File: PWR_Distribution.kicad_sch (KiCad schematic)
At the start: 33 parts, among them IC4 AP64501QSP-13, IC8 LM76202QPWPRQ1, J1 CarPowerConnector

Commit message: fixed erc and removed old schematics
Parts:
- IC8: Arrow Part Number (none) -> LM76202QPWPRQ1; Arrow Price/Stock (none) -> https://www.arrow.com/en/products/lm76202qpwprq1/texas-inst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; Height (none) -> 1.2; Manufacturer_Name (none) -> Texas Instruments; Manufacturer_Part_Number (none) -> LM76202QPWPRQ1; Mouser Part Number (none) -> 595-LM76202QPWPRQ1; Mouser Price/Stock (none) -> https://www.mouser.co.uk/ProductDetail/Texas-Instruments/LM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

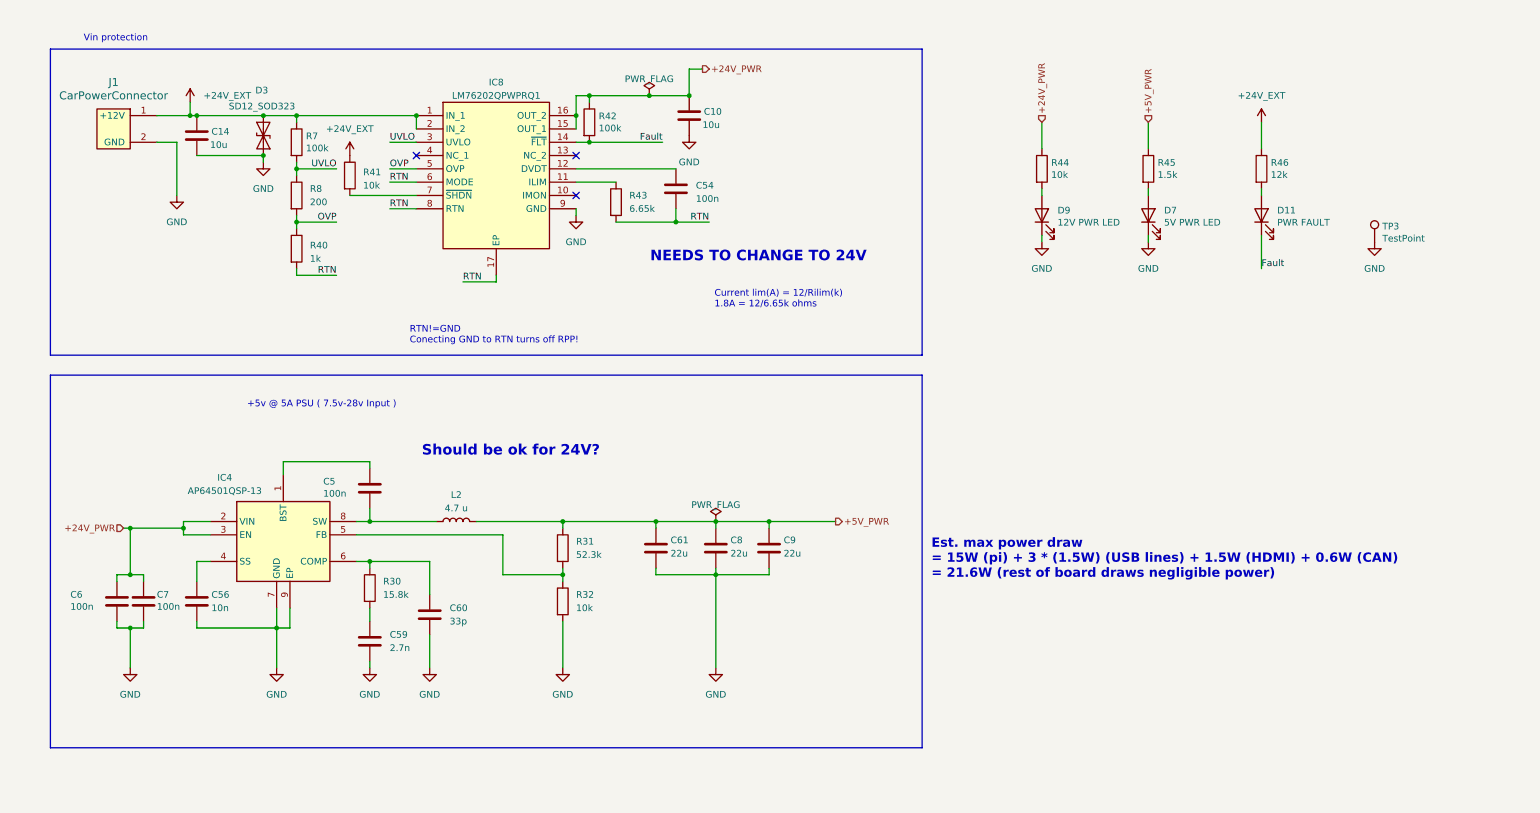
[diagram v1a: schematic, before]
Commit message: updated power to 24V i think
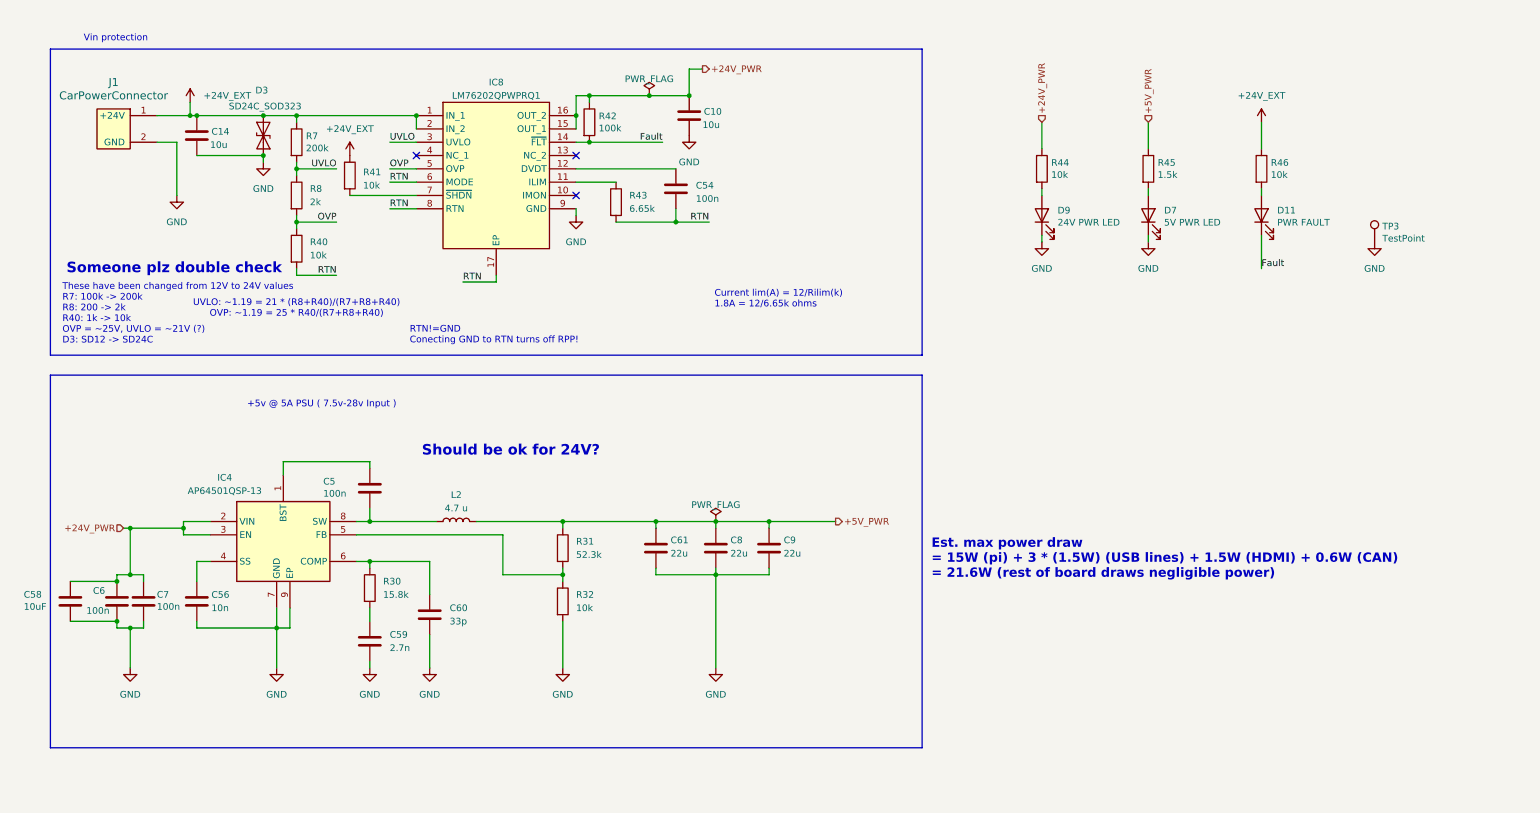
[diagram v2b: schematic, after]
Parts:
- added C58: 10uF, Capacitor_SMD:C_0805_2012Metric, symbol Device:C
- D3: value SD12_SOD323 -> SD24C_SOD323; P/N PESD15VL1BA,115 -> SD24C-01FTG
- D9: value 12V PWR LED -> 24V PWR LED
- R40: value 1k -> 10k
- R46: value 12k -> 10k
- R7: value 100k -> 200k
- R8: value 200 -> 2k
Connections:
- net +24V_PWR: now also C58.1
- net GND: now also C58.2
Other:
- note added: "Someone plz double check"
- note added: "These have been changed from 12V to 24V values R7: 100k -> 200k R8: 200 -> 2k R40: 1k -> 10k OVP = ~25V, UVLO = ~21V (?) D3: SD12 -> SD24C"
- note added: "UVLO: ~1.19 = 21 * (R8+R40)/(R7+R8+R40) OVP: ~1.19 = 25 * R40/(R7+R8+R40)"
- note removed: "NEEDS TO CHANGE TO 24V"
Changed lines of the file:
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@@
 		)
 	)
+	(text "UVLO: ~1.19 = 21 * (R8+R40)/(R7+R8+R40)\nOVP: ~1.19 = 25 * R40/(R7+R8+R40)"
+		(exclude_from_sim no)
+		(at 67.31 74.93 0)
+		(effects
+			(font
+				(size 1.27 1.27)
+			)
+		)
+	)
+	(text "These have been changed from 12V to 24V values\nR7: 100k -> 200k\nR8: 200 -> 2k\nR40: 1k -> 10k\nOVP = ~25V, UVLO = ~21V (?)\nD3: SD12 -> SD24C"
+		(exclude_from_sim no)
+		(at 22.606 75.946 0)
+		(effects
+			(font
+				(size 1.27 1.27)
+			)
+			(justify left)
+		)
+	)
 	(text "Est. max power draw \n= 15W (pi) + 3 * (1.5W) (USB lines) + 1.5W (HDMI) + 0.6W (CAN) \n= 21.6W (rest of board draws negligible power)\n"
 		(exclude_from_sim no)
@@
 		)
 	)
-	(text "NEEDS TO CHANGE TO 24V"
+	(text "Someone plz double check\n"
 		(exclude_from_sim no)
-		(at 155.448 65.024 0)
+		(at 43.942 67.31 0)
 		(effects
 			(font
@@
 	)
 	(junction
+		(at 33.02 134.62)
+		(diameter 0)
+		(color 0 0 0 0)
+	)
+	(junction
 		(at 45.72 116.84)
 		(diameter 0)
@@
 	)
 	(junction
+		(at 33.02 127)
+		(diameter 0)
+		(color 0 0 0 0)
+	)
+	(junction
 		(at 134.62 34.29)
 		(diameter 0)
@@
 	(wire
 		(pts
+			(xy 24.13 127) (xy 33.02 127)
+		)
+		(stroke
+			(width 0)
+			(type default)
+		)
+	)
+	(wire
+		(pts
 			(xy 134.62 34.29) (xy 142.24 34.29)
 		)
@@
 	(wire
 		(pts
+			(xy 24.13 134.62) (xy 33.02 134.62)
+		)
+		(stroke
+			(width 0)
+			(type default)
+		)
+	)
+	(wire
+		(pts
 			(xy 67.31 67.31) (xy 67.31 68.58)
 		)
@@
 			)
 		)
-		(property "Value" "100k"
+		(property "Value" "200k"
 			(at 69.088 44.323 0)
 			(effects
@@
 			)
 		)
-		(property "Value" "12V PWR LED"
+		(property "Value" "24V PWR LED"
 			(at 212.5472 58.4962 90)
 			(effects
@@
 			)
 		)
-		(property "Value" "200"
+		(property "Value" "2k"
 			(at 69.85 54.6099 0)
 			(effects
@@
 			)
 		)
-		(property "Value" "SD12_SOD323"
+		(property "Value" "SD24C_SOD323"
 			(at 54.356 36.322 90)
 			(effects
@@
 			)
 		)
-		(property "Description" "12V, 450W Discrete Bidirectional TVS Diode, SOD-323"
+		(property "Description" "24V, 450W Discrete Bidirectional TVS Diode, SOD-323-2"
 			(at 60.96 41.91 0)
 			(effects
@@
 			)
 		)
-		(property "P/N" "PESD15VL1BA,115"
+		(property "P/N" "SD24C-01FTG"
 			(at 60.96 41.91 90)
 			(effects
@@
 		(fields_autoplaced yes)
 		(property "Reference" "R40"
-			(at 69.85 62.865 0)
+			(at 69.85 62.2299 0)
 			(effects
 				(font
@@
 			)
 		)
-		(property "Value" "1k"
-			(at 69.85 65.405 0)
+		(property "Value" "10k"
+			(at 69.85 64.7699 0)
 			(effects
 				(font
@@
 			)
 		)
-		(property "Value" "12k"
+		(property "Value" "10k"
 			(at 253.238 49.403 0)
 			(effects
@@
 		(dnp no)
 		(property "Reference" "C6"
-			(at 24.13 129.5146 0)
+			(at 28.448 128.778 0)
 			(effects
 				(font
@@
 		)
 		(property "Value" "100n"
-			(at 24.13 131.826 0)
+			(at 27.178 132.588 0)
 			(effects
 				(font
@@
 					(unit 1)
 				)
+			)
+		)
+	)
+	(symbol
+		(lib_id "Device:C")
+		(at 24.13 130.81 0)
+		(unit 1)
+		(exclude_from_sim no)
+		(in_bom yes)
+		(on_board yes)
+		(dnp no)
+		(property "Reference" "C58"
+			(at 15.24 129.5146 0)
+			(effects
+				(font
+					(size 1.27 1.27)
+				)
+				(justify left)
+			)
+		)
+		(property "Value" "10uF"
+			(at 15.24 131.826 0)
+			(effects
+				(font
+					(size 1.27 1.27)
+				)
+				(justify left)
+			)
+		)
+		(property "Footprint" "Capacitor_SMD:C_0805_2012Metric"
+			(at 25.0952 134.62 0)
+			(effects
+				(font
+					(size 1.27 1.27)
+				)
+				(hide yes)
+			)
+		)
+		(property "Datasheet" "~"
+			(at 24.13 130.81 0)
+			(effects
+				(font
+					(size 1.27 1.27)
+				)
+				(hide yes)
+			)
+		)
+		(property "Description" "Unpolarized capacitor"
+			(at 24.13 130.81 0)
+			(effects
+				(font
+					(size 1.27 1.27)
+				)
+				(hide yes)
+			)
+		)
+		(property "P/N" "0805W106K500CC"
+			(at 24.13 130.81 0)
+			(effects
+				(font
+					(size 1.27 1.27)
+				)
+				(hide yes)
+			)
+		)
+		(pin "1"
+		)
+		(pin "2"
+		)
+		(instances
+			(project "PiBoard"
+				(path "/e4d65698-b8ec-4bf6-9f2b-a5010377155a/0c1fd794-8ba7-4f58-ad3e-1ee234c84a43"
+					(reference "C58")
+					(unit 1)
+				)

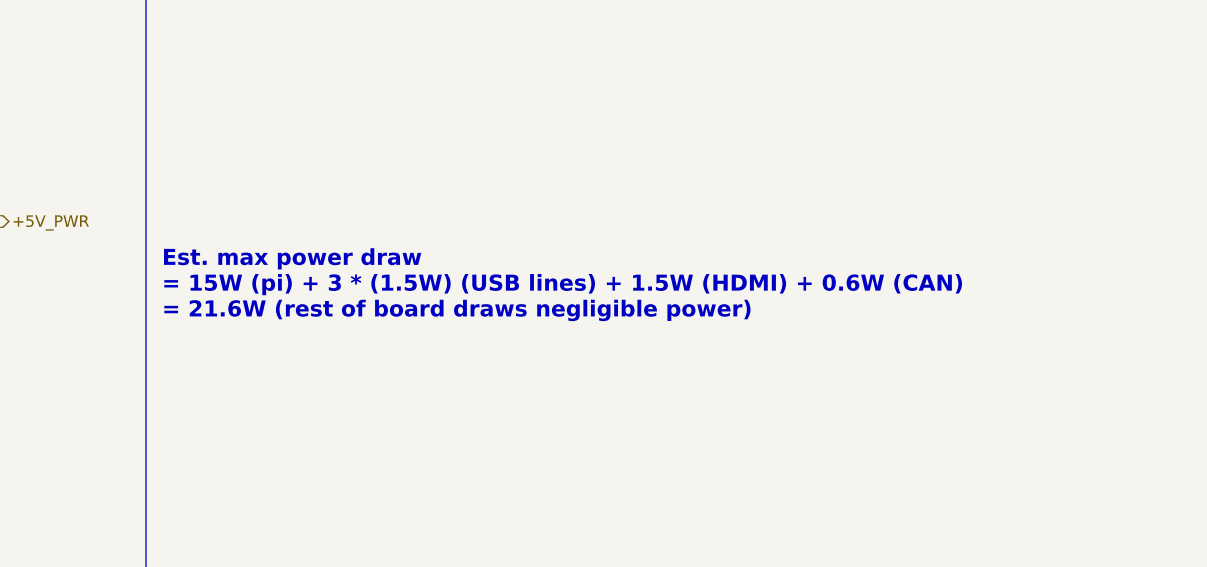
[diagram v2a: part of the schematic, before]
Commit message: changed usb to be simpler (no inbuilt hub)
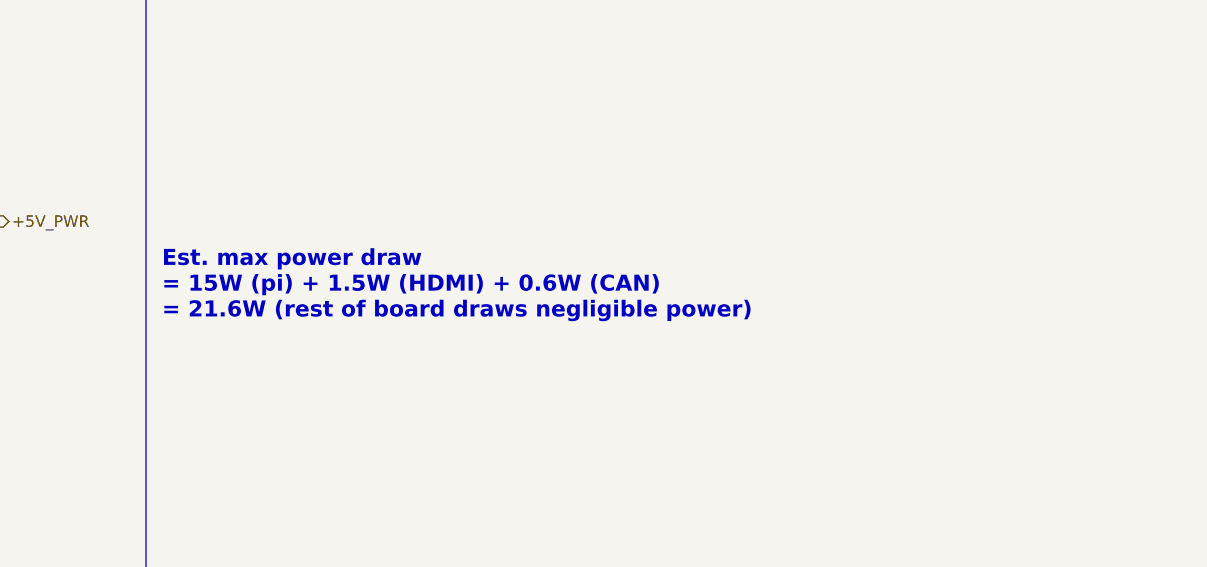
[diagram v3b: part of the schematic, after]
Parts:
- IC4: Height 1.63 -> (none); Manufacturer_Name Diodes Incorporated -> (none); Manufacturer_Part_Number AP64501QSP-13 -> (none); Mouser Part Number 621-AP64501QSP-13 -> (none); Mouser Price/Stock https://www.mouser.co.uk/ProductDetail/Diodes-Incorporated/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 -> (none)
- IC8: Arrow Part Number LM76202QPWPRQ1 -> (none); Arrow Price/Stock https://www.arrow.com/en/products/lm76202qpwprq1/texas-inst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 -> (none); Height 1.2 -> (none); Manufacturer_Name Texas Instruments -> (none); Manufacturer_Part_Number LM76202QPWPRQ1 -> (none); Mouser Part Number 595-LM76202QPWPRQ1 -> (none); Mouser Price/Stock https://www.mouser.co.uk/ProductDetail/Texas-Instruments/LM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 -> (none)
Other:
- note added: "Est. max power draw = 15W (pi) + 1.5W (HDMI) + 0.6W (CAN) = 21.6W (rest of board draws negligible power)"
- note removed: "Est. max power draw = 15W (pi) + 3 * (1.5W) (USB lines) + 1.5W (HDMI) + 0.6W (CAN) = 21.6W (rest of board draws negligible power)"
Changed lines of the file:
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@@
 		)
 	)
-	(text "Est. max power draw \n= 15W (pi) + 3 * (1.5W) (USB lines) + 1.5W (HDMI) + 0.6W (CAN) \n= 21.6W (rest of board draws negligible power)\n"
+	(text "Est. max power draw \n= 15W (pi) + 1.5W (HDMI) + 0.6W (CAN) \n= 21.6W (rest of board draws negligible power)\n"
 		(exclude_from_sim no)
 		(at 188.468 122.682 0)
@@
 			)
 		)
-		(property "Datasheet" "~"
+		(property "Datasheet" ""
 			(at 81.28 109.22 0)
 			(effects
@@
 			)
 		)
-		(property "Height" "1.2"
-			(at 116.84 433.02 0)
-			(effects
-				(font
-					(size 1.27 1.27)
-				)
-				(justify left top)
-				(hide yes)
-			)
-		)
-		(property "Manufacturer_Name" "Texas Instruments"
-			(at 116.84 533.02 0)
-			(effects
-				(font
-					(size 1.27 1.27)
-				)
-				(justify left top)
-				(hide yes)
-			)
-		)
-		(property "Manufacturer_Part_Number" "LM76202QPWPRQ1"
-			(at 116.84 633.02 0)
-			(effects
-				(font
-					(size 1.27 1.27)
-				)
-				(justify left top)
-				(hide yes)
-			)
-		)
-		(property "Mouser Part Number" "595-LM76202QPWPRQ1"
-			(at 116.84 733.02 0)
-			(effects
-				(font
-					(size 1.27 1.27)
-				)
-				(justify left top)
-				(hide yes)
-			)
-		)
-		(property "Mouser Price/Stock" "https://www.mouser.co.uk/ProductDetail/Texas-Instruments/LM76202QPWPRQ1?qs=B6kkDfuK7%2FDO3IObrBgfZg%3D%3D"
-			(at 116.84 833.02 0)
-			(effects
-				(font
-					(size 1.27 1.27)
-				)
-				(justify left top)
-				(hide yes)
-			)
-		)
-		(property "Arrow Part Number" "LM76202QPWPRQ1"
-			(at 116.84 933.02 0)
-			(effects
-				(font
-					(size 1.27 1.27)
-				)
-				(justify left top)
-				(hide yes)
-			)
-		)
-		(property "Arrow Price/Stock" "https://www.arrow.com/en/products/lm76202qpwprq1/texas-instruments"
-			(at 116.84 1033.02 0)
-			(effects
-				(font
-					(size 1.27 1.27)
-				)
-				(justify left top)
-				(hide yes)
-			)
-		)
 		(pin "12"
 		)
@@
 			)
 		)
-		(property "Datasheet" "~"
+		(property "Datasheet" ""
 			(at 38.1 130.81 0)
 			(effects
@@
 			)
 		)
-		(property "Height" "1.63"
-			(at 77.47 509.22 0)
-			(effects
-				(font
-					(size 1.27 1.27)
-				)
-				(justify left top)
-				(hide yes)
-			)
-		)
-		(property "Manufacturer_Name" "Diodes Incorporated"
-			(at 77.47 609.22 0)
-			(effects
-				(font
-					(size 1.27 1.27)
-				)
-				(justify left top)
-				(hide yes)
-			)
-		)
-		(property "Manufacturer_Part_Number" "AP64501QSP-13"
-			(at 77.47 709.22 0)
-			(effects
-				(font
-					(size 1.27 1.27)
-				)
-				(justify left top)
-				(hide yes)
-			)
-		)
-		(property "Mouser Part Number" "621-AP64501QSP-13"
-			(at 77.47 809.22 0)
-			(effects
-				(font
-					(size 1.27 1.27)
-				)
-				(justify left top)
-				(hide yes)
-			)
-		)
-		(property "Mouser Price/Stock" "https://www.mouser.co.uk/ProductDetail/Diodes-Incorporated/AP64501QSP-13?qs=IS%252B4QmGtzzqtXRaIlE2s%2FA%3D%3D"
-			(at 77.47 909.22 0)
-			(effects
-				(font
-					(size 1.27 1.27)
-				)
-				(justify left top)
-				(hide yes)
-			)
-		)
-		(property "Arrow Part Number" ""
-			(at 77.47 1009.22 0)
-			(effects
-				(font
-					(size 1.27 1.27)
-				)
-				(justify left top)
-				(hide yes)
-			)
-		)
-		(property "Arrow Price/Stock" ""
-			(at 77.47 1109.22 0)
-			(effects
-				(font
-					(size 1.27 1.27)
-				)
-				(justify left top)
-				(hide yes)
-			)
-		)
 		(pin "9"
 		)
@@
 			)
 		)
-		(property "Datasheet" "~"
+		(property "Datasheet" ""
 			(at 33.02 130.81 0)
 			(effects

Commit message: moved everything to front & 0603'd stuff
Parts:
- C5, C54, C56, C59, C6, C60, C61, C7, C8, C9: footprint Capacitor_SMD:C_0805_2012Metric -> Capacitor_SMD:C_0603_1608Metric
- D11, D7, D9: footprint LED_SMD:LED_0805_2012Metric -> LED_SMD:LED_0603_1608Metric
- J1: footprint Connector_Molex:Molex_Micro-Fit_3.0_43650-0215_1x02_P3.00mm_Vertical -> UTSVT_Connectors:Molex_Nano-Fit_105309-xx02_1x02_P2.50mm_Vertical
- R45: footprint Resistor_SMD:R_0805_2012Metric -> Resistor_SMD:R_0603_1608Metric
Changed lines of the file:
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@@
 			)
 		)
-		(property "Footprint" "Capacitor_SMD:C_0805_2012Metric"
+		(property "Footprint" "Capacitor_SMD:C_0603_1608Metric"
 			(at 93.6752 137.16 0)
 			(effects
@@
 			)
 		)
-		(property "Footprint" "Resistor_SMD:R_0805_2012Metric"
+		(property "Footprint" "Resistor_SMD:R_0603_1608Metric"
 			(at 228.092 48.26 90)
 			(effects
@@
 			)
 		)
-		(property "Footprint" "LED_SMD:LED_0805_2012Metric"
+		(property "Footprint" "LED_SMD:LED_0603_1608Metric"
 			(at 209.55 57.15 0)
 			(effects
@@
 			)
 		)
-		(property "Footprint" "Capacitor_SMD:C_0805_2012Metric"
+		(property "Footprint" "Capacitor_SMD:C_0603_1608Metric"
 			(at 148.2852 124.46 0)
 			(effects
@@
 			)
 		)
-		(property "Footprint" "Capacitor_SMD:C_0805_2012Metric"
+		(property "Footprint" "Capacitor_SMD:C_0603_1608Metric"
 			(at 49.2252 134.62 0)
 			(effects
@@
 			)
 		)
-		(property "Footprint" "LED_SMD:LED_0805_2012Metric"
+		(property "Footprint" "LED_SMD:LED_0603_1608Metric"
 			(at 251.46 57.15 0)
 			(effects
@@
 			)
 		)
-		(property "Footprint" "Capacitor_SMD:C_0805_2012Metric"
+		(property "Footprint" "Capacitor_SMD:C_0603_1608Metric"
 			(at 82.2452 113.03 0)
 			(effects
@@
 			)
 		)
-		(property "Footprint" "Capacitor_SMD:C_0805_2012Metric"
+		(property "Footprint" "Capacitor_SMD:C_0603_1608Metric"
 			(at 140.6652 55.88 0)
 			(effects
@@
 			)
 		)
-		(property "Footprint" "Capacitor_SMD:C_0805_2012Metric"
+		(property "Footprint" "Capacitor_SMD:C_0603_1608Metric"
 			(at 82.2452 142.24 0)
 			(effects
@@
 			)
 		)
-		(property "Footprint" "Connector_Molex:Molex_Micro-Fit_3.0_43650-0215_1x02_P3.00mm_Vertical"
+		(property "Footprint" "UTSVT_Connectors:Molex_Nano-Fit_105309-xx02_1x02_P2.50mm_Vertical"
 			(at 33.02 40.64 0)
 			(effects
@@
 			)
 		)
-		(property "Footprint" "LED_SMD:LED_0805_2012Metric"
+		(property "Footprint" "LED_SMD:LED_0603_1608Metric"
 			(at 229.87 57.15 0)
 			(effects
@@
 			)
 		)
-		(property "Footprint" "Capacitor_SMD:C_0805_2012Metric"
+		(property "Footprint" "Capacitor_SMD:C_0603_1608Metric"
 			(at 39.0652 134.62 0)
 			(effects
@@
 			)
 		)
-		(property "Footprint" "Capacitor_SMD:C_0805_2012Metric"
+		(property "Footprint" "Capacitor_SMD:C_0603_1608Metric"
 			(at 158.4452 124.46 0)
 			(effects
@@
 			)
 		)
-		(property "Footprint" "Capacitor_SMD:C_0805_2012Metric"
+		(property "Footprint" "Capacitor_SMD:C_0603_1608Metric"
 			(at 136.8552 124.46 0)
 			(effects
@@
 			)
 		)
-		(property "Footprint" "Capacitor_SMD:C_0805_2012Metric"
+		(property "Footprint" "Capacitor_SMD:C_0603_1608Metric"
 			(at 33.9852 134.62 0)
 			(effects
